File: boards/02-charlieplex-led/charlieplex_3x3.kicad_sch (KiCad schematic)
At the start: 14 parts, among them U1 MCU

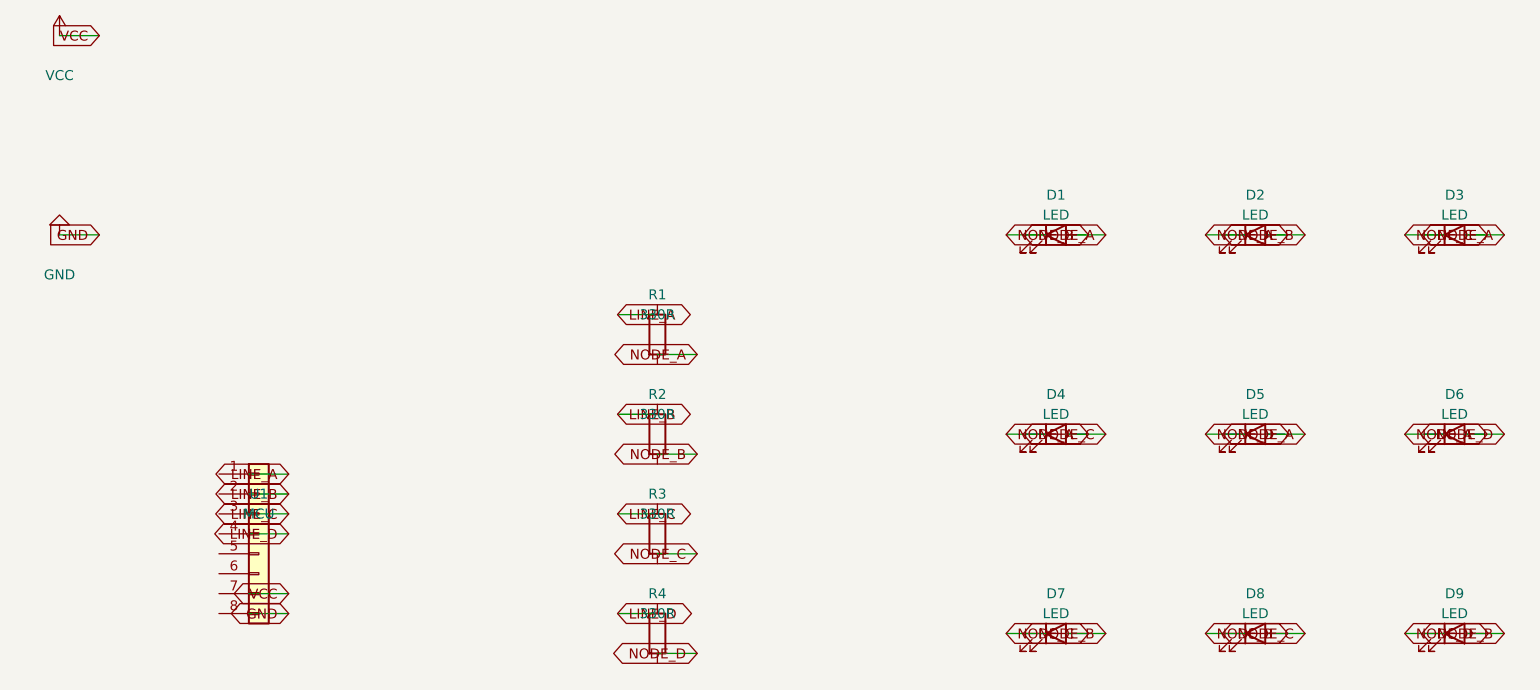
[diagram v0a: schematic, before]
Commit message: feat(schematic): Add no_connect marker support and fix charlieplex ERC errors
- Add NoConnect element class for marking intentionally unconnected pins
- Add add_no_connect() method to schematic API
- Add no_connect_node builder function for S-expression serialization
- Update charlieplex generate_schematic.py to:
  - Add PWR_FLAG symbols for VCC and GND power nets
  - Add no-connect markers for NC pins (5 and 6) on MCU
- Schematic now passes kct sch validate with no ERC errors

Closes #654

Co-Authored-By: Claude Opus 4.5 <noreply@anthropic.com>
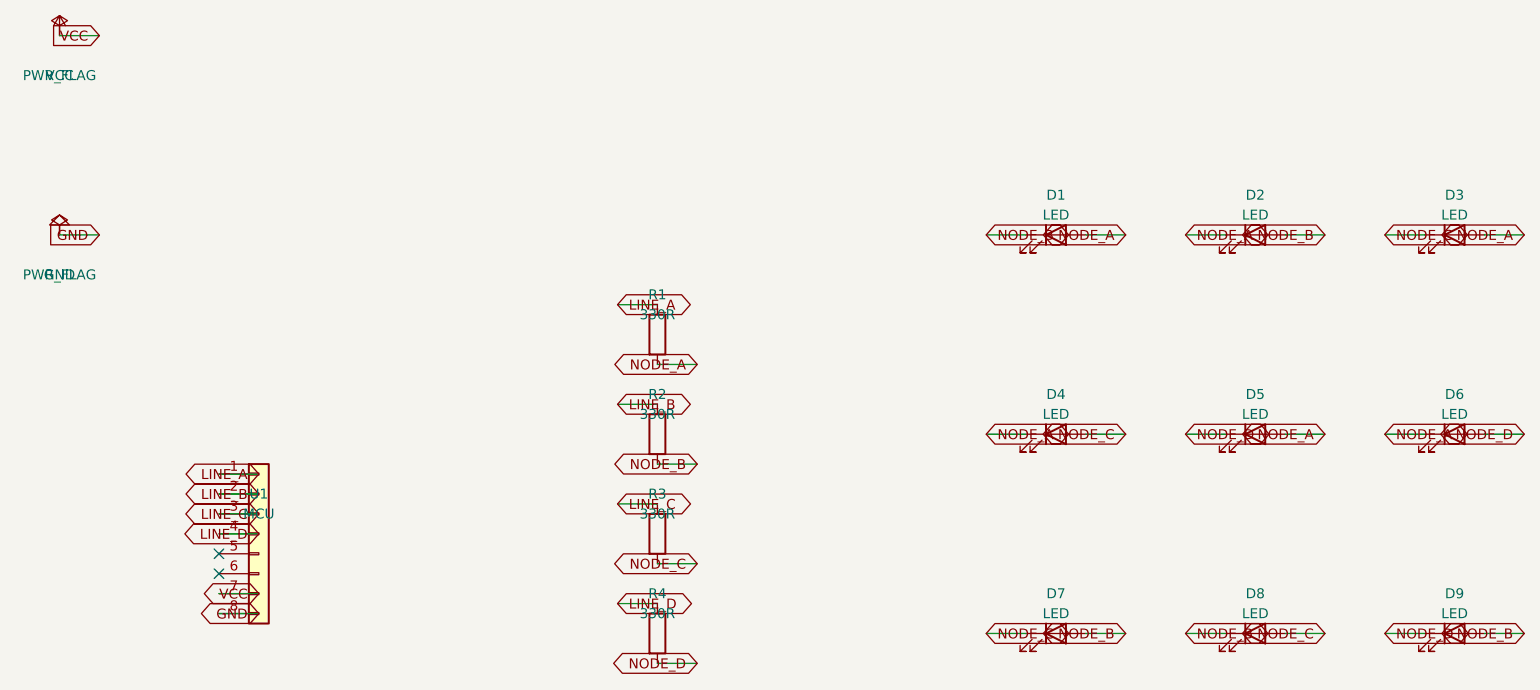
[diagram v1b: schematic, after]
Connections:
- net GND: now also U1.8 (Pin_8)
- net LINE_A: now also R1.1, U1.1 (Pin_1)
- net LINE_B: now also R2.1, U1.2 (Pin_2)
- net LINE_C: now also R3.1, U1.3 (Pin_3)
- net LINE_D: now also R4.1, U1.4 (Pin_4)
- net NODE_A: now also D1.2 (A), D2.1 (K), D3.2 (A), D4.1 (K), D5.2 (A), D6.1 (K), R1.2
- net NODE_B: now also D1.1 (K), D2.2 (A), D7.2 (A), D8.1 (K), D9.2 (A), R2.2
- net NODE_C: now also D3.1 (K), D4.2 (A), D7.1 (K), D8.2 (A), R3.2
- net NODE_D: now also D5.1 (K), D6.2 (A), D9.1 (K), R4.2
- net VCC: now also U1.7 (Pin_7)
- no-connect marks 0 -> 2

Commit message: fix(examples): Add footprint assignments to schematic examples (#678)
Update the charlieplex and voltage divider example scripts to use the
existing `footprint` and `auto_footprint` parameters in add_symbol().

Changes:
- charlieplex: Add explicit footprint for MCU connector, auto_footprint
  for resistors, and explicit footprints for LEDs
- voltage_divider: Add explicit footprints for connectors and
  auto_footprint for resistors
- Regenerated output files with footprint assignments

The `footprint` parameter and `auto_footprint` feature already existed
in add_symbol() - the examples just weren't using them, which caused
"Missing footprint" warnings during schematic validation.

Closes #678

Co-Authored-By: Claude Opus 4.5 <noreply@anthropic.com>
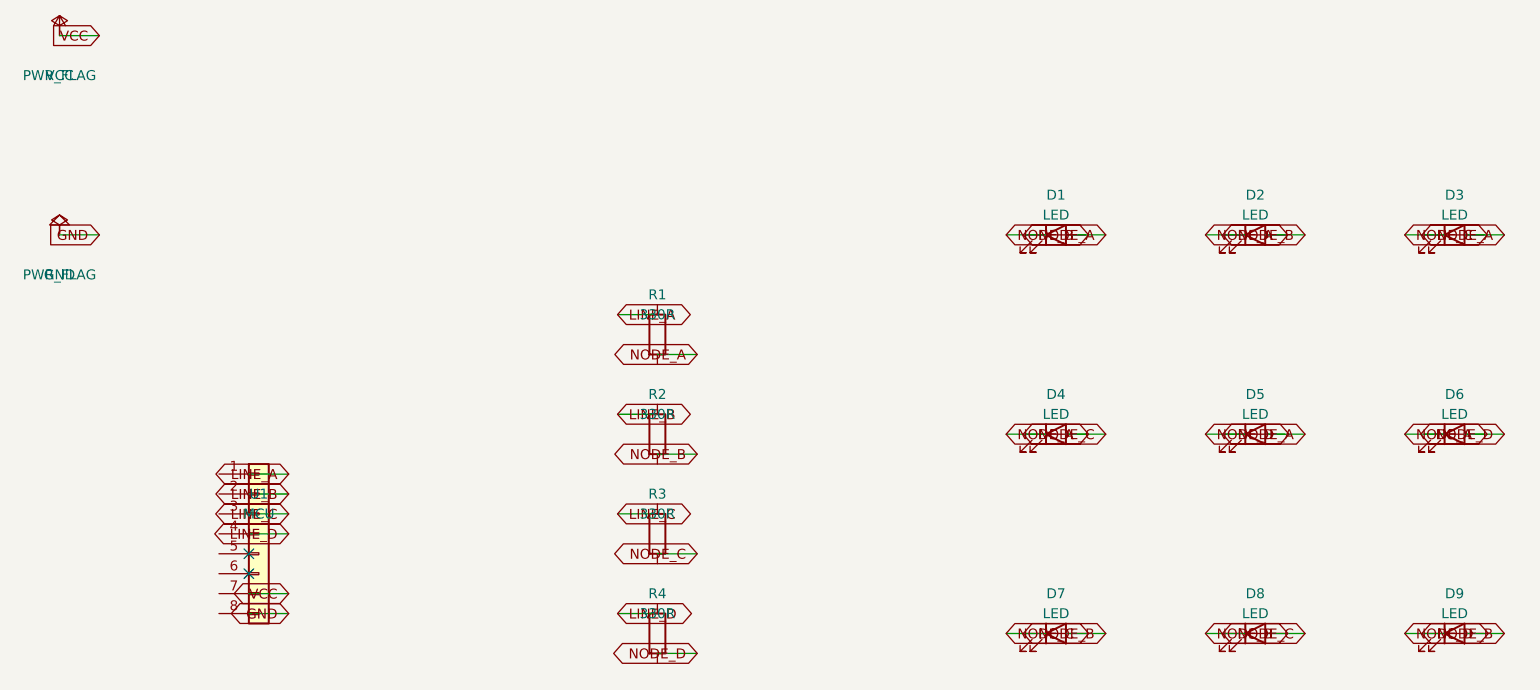
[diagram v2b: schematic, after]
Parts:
- D1, D2, D3, D4, D5, D6, D7, D8, D9: footprint (none) -> LED_SMD:LED_0805_2012Metric
- R1, R2, R3, R4: footprint (none) -> Resistor_SMD:R_0402_1005Metric
- U1: footprint (none) -> Connector_PinHeader_2.54mm:PinHeader_1x08_P2.54mm_Vertical
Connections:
- net GND: no longer U1.8 (Pin_8)
- net LINE_A: no longer R1.1, U1.1 (Pin_1)
- net LINE_B: no longer R2.1, U1.2 (Pin_2)
- net LINE_C: no longer R3.1, U1.3 (Pin_3)
- net LINE_D: no longer R4.1, U1.4 (Pin_4)
- net NODE_A: no longer D1.2 (A), D2.1 (K), D3.2 (A), D4.1 (K), D5.2 (A), D6.1 (K), R1.2
- net NODE_B: no longer D1.1 (K), D2.2 (A), D7.2 (A), D8.1 (K), D9.2 (A), R2.2
- net NODE_C: no longer D3.1 (K), D4.2 (A), D7.1 (K), D8.2 (A), R3.2
- net NODE_D: no longer D5.1 (K), D6.2 (A), D9.1 (K), R4.2
- net VCC: no longer U1.7 (Pin_7)

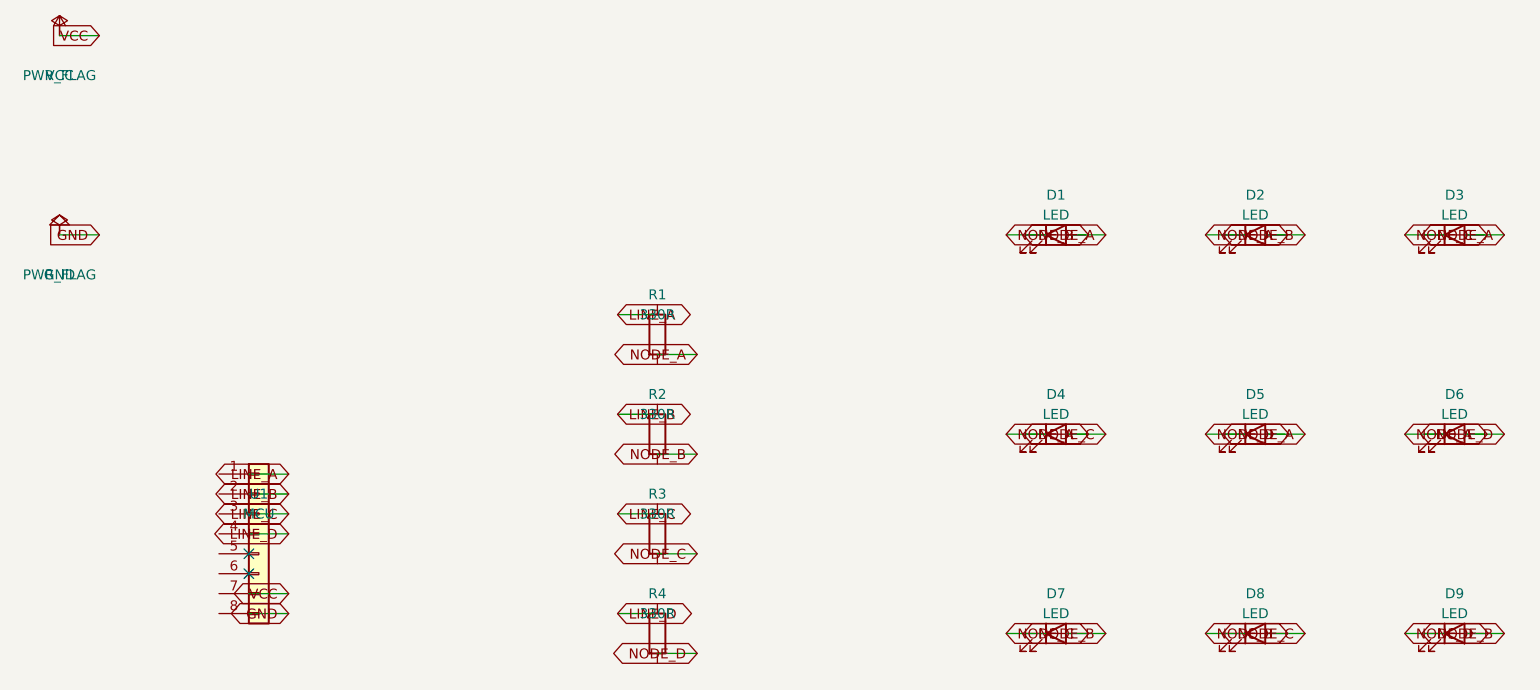
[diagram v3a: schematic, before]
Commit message: fix(schematic): Correct pin connection_point to return wire position
The Pin.connection_point() method was incorrectly calculating the wire
connection point by adding the pin length at the specified angle.
In KiCad's schematic format, the pin's (at x y angle) specifies the
endpoint where wires connect - the connection point IS the (x, y)
position directly.

This fixes ERC validation errors in demo schematics where wires
were being placed at the wrong position relative to component pins.

Regenerated demo schematics with correct wire positions.

Closes #700

Co-Authored-By: Claude Opus 4.5 <noreply@anthropic.com>
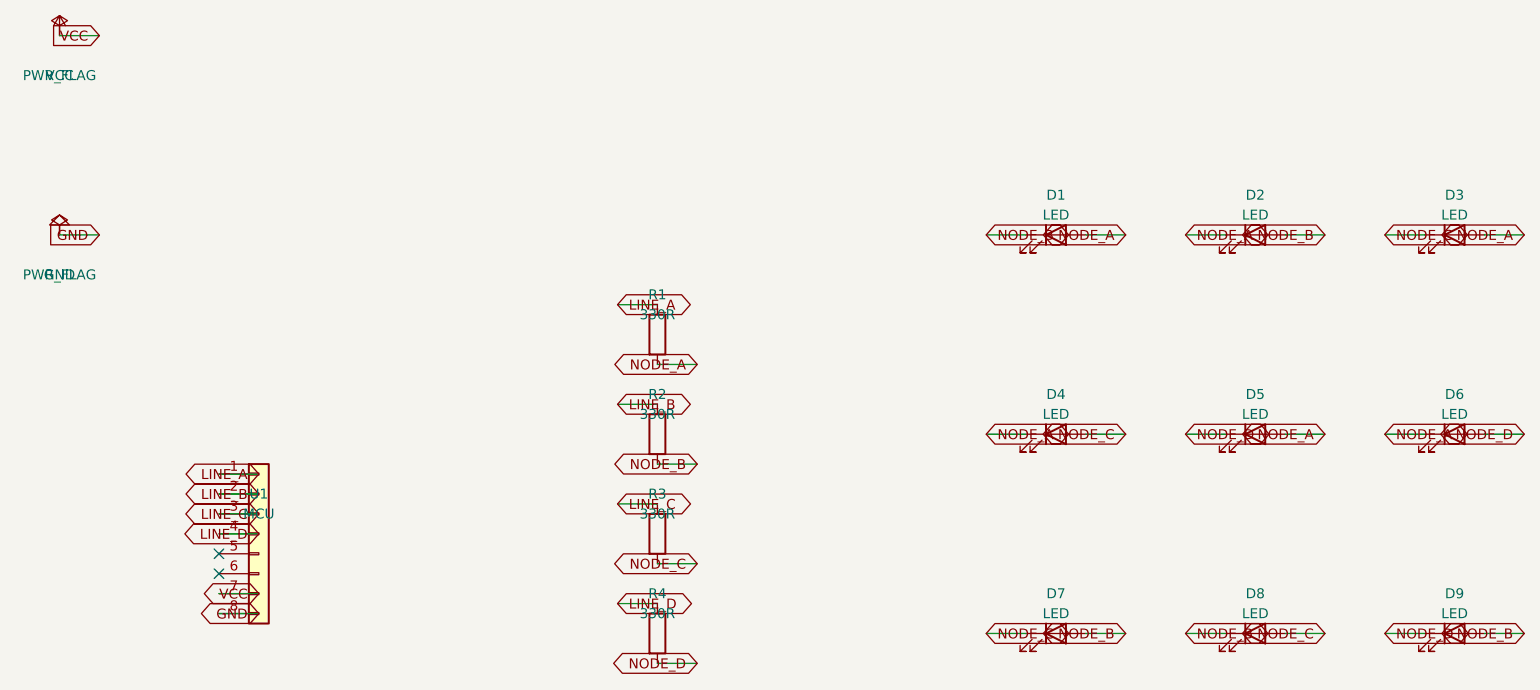
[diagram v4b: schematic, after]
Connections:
- net GND: now also U1.8 (Pin_8)
- net LINE_A: now also R1.1, U1.1 (Pin_1)
- net LINE_B: now also R2.1, U1.2 (Pin_2)
- net LINE_C: now also R3.1, U1.3 (Pin_3)
- net LINE_D: now also R4.1, U1.4 (Pin_4)
- net NODE_A: now also D1.2 (A), D2.1 (K), D3.2 (A), D4.1 (K), D5.2 (A), D6.1 (K), R1.2
- net NODE_B: now also D1.1 (K), D2.2 (A), D7.2 (A), D8.1 (K), D9.2 (A), R2.2
- net NODE_C: now also D3.1 (K), D4.2 (A), D7.1 (K), D8.2 (A), R3.2
- net NODE_D: now also D5.1 (K), D6.2 (A), D9.1 (K), R4.2
- net VCC: now also U1.7 (Pin_7)
